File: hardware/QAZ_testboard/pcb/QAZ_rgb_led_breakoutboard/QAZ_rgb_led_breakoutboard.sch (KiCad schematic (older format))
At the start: 25 parts, among them J1 Conn_01x01_Male, J2 Conn_01x01_Male, J3 Conn_01x01_Male, J4 Conn_01x01_Male, J5 Conn_01x01_Male, J6 Conn_01x03_Male, J7 Conn_01x03_Male, J8 Conn_01x03_Male, U1 LP5009RUKR

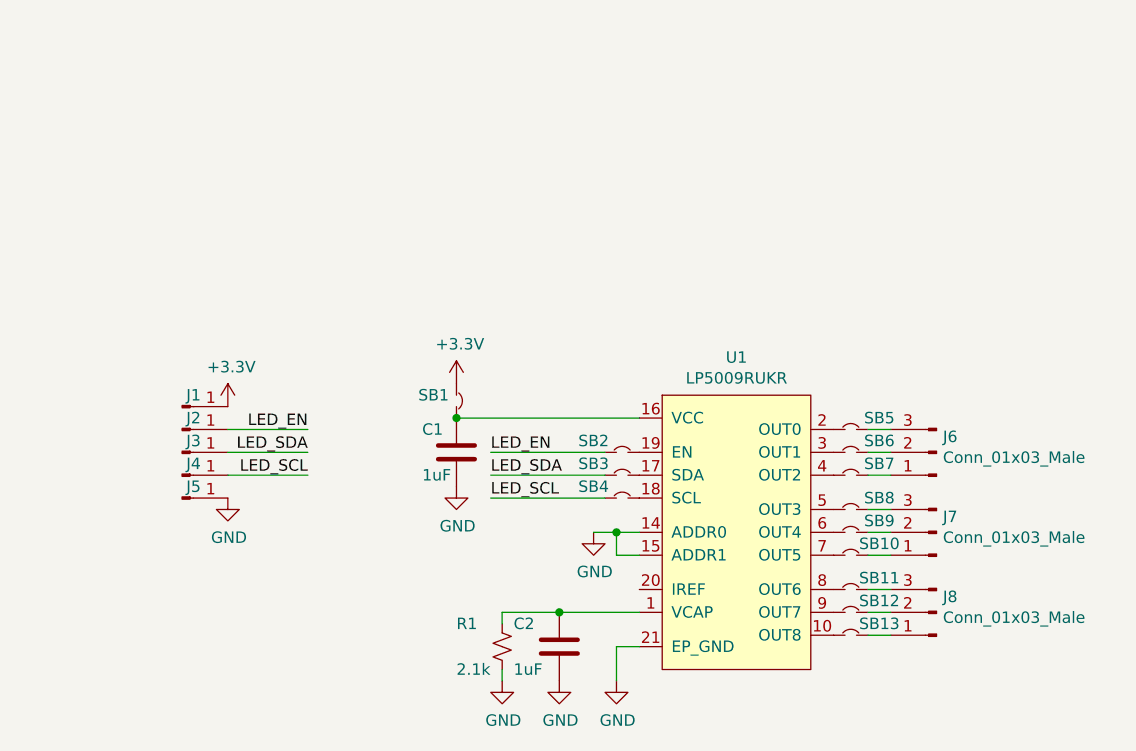
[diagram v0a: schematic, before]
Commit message: breakout: rgb conversion board
Made a conversion board for the LED driver conversion board. The RGB
LEDs chosen will not fit, and must be replaced in QAZ v1.1.
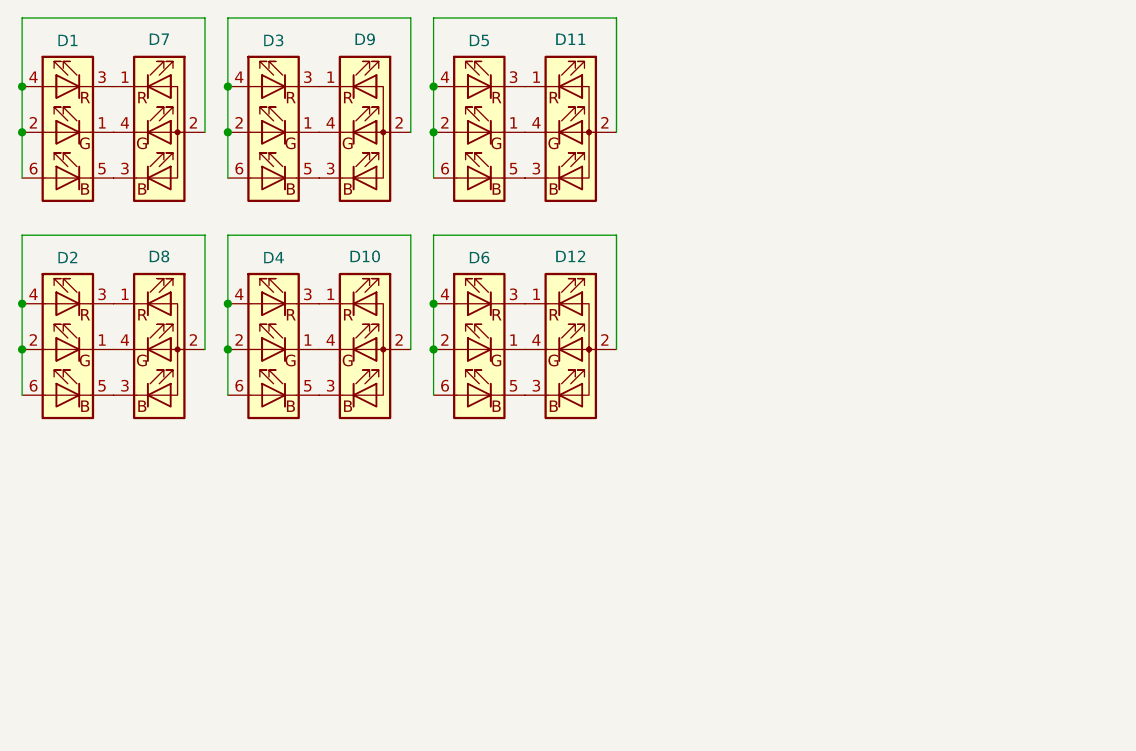
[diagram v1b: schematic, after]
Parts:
- removed C1, C2: 1uF, Capacitor_SMD:C_0603_1608Metric_Pad1.05x0.95mm_HandSolder, symbol Device:C
- removed J1, J2, J3, J4, J5: Conn_01x01_Male, Connector_PinHeader_1.00mm:PinHeader_1x01_P1.00mm_Vertical, symbol Connector:Conn_01x01_Male
- removed J6, J7, J8: Conn_01x03_Male, Connector_PinHeader_1.00mm:PinHeader_1x03_P1.00mm_Vertical, symbol Connector:Conn_01x03_Male
- removed R1: 2.1k, Resistor_SMD:R_0603_1608Metric_Pad1.05x0.95mm_HandSolder, symbol Device:R_Small_US
- removed SB1, SB10, SB11, SB12, SB13, SB2, SB3, SB4, SB5, SB6, SB7, SB8, SB9: SolderBridge, Resistor_SMD:R_0603_1608Metric_Pad1.05x0.95mm_HandSolder, symbol QAZ:SolderBridge
- removed U1: LP5009RUKR, QAZ:QFN-20-1EP_3x3mm_P0.4mm_EP1.65x1.65mm_HS, symbol QAZ:LP5009RUKR
- added D1, D2, D3, D4, D5, D6: 19-337C_RSBHGHC-A88_4T, QAZ:0606_1616Metric_HS, symbol QAZ:19-337C_RSBHGHC-A88_4T
- added D10, D11, D12, D7, D8, D9: LED_RABG, LED_THT:LED_D5.0mm-4_RGB, symbol Device:LED_RABG
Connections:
- new net: D1.3, D7.1 (RK)
- new net: D1.2, D1.4, D1.6, D7.2 (A)
- new net: D1.5, D7.3 (BK)
- new net: D1.1, D7.4 (GK)
- new net: D2.3, D8.1 (RK)
- new net: D2.2, D2.4, D2.6, D8.2 (A)
- new net: D2.5, D8.3 (BK)
- new net: D2.1, D8.4 (GK)
- new net: D3.3, D9.1 (RK)
- new net: D3.2, D3.4, D3.6, D9.2 (A)
- new net: D3.5, D9.3 (BK)
- new net: D3.1, D9.4 (GK)
- new net: D10.1 (RK), D4.3
- new net: D10.2 (A), D4.2, D4.4, D4.6
- new net: D10.3 (BK), D4.5
- new net: D10.4 (GK), D4.1
- new net: D11.1 (RK), D5.3
- new net: D11.2 (A), D5.2, D5.4, D5.6
- new net: D11.3 (BK), D5.5
- new net: D11.4 (GK), D5.1
- new net: D12.1 (RK), D6.3
- new net: D12.2 (A), D6.2, D6.4, D6.6
- new net: D12.3 (BK), D6.5
- new net: D12.4 (GK), D6.1
